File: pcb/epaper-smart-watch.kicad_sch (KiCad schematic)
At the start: 64 parts, among them J1 AXT624124, J3 Lithium Battery 3.7V, M1 Motor_DC, P1 USB_C_Plug_USB2.0, Q1 MMBT3904, Q3 Si1308EDL, SW1 BTN, SW2 BTN, SW3 BTN, SW4 BTN, U1 CH340E, U2 STM32WB1MMCH6TR, U3 LSM6DS3

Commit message: V2 soon...
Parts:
- removed C12: 4.7uF, Capacitor_SMD:C_0402_1005Metric, symbol Device:C_Small
- removed C13: 2.2uF, Capacitor_SMD:C_0402_1005Metric, symbol Device:C_Small
- removed C14: 1uF, Capacitor_SMD:C_0402_1005Metric, symbol Device:C_Small
- removed C15, C17, C9: 0.1uF, Capacitor_SMD:C_0402_1005Metric, symbol Device:C_Small
- removed C18: 10uF, Capacitor_SMD:C_0402_1005Metric, symbol Device:C_Small
- removed C19, C20, C21: 2.7pF, Capacitor_SMD:C_0402_1005Metric, symbol Device:C_Small
- removed D1, D3, D4: LESD5D5.0CT1G, SamacSys:LESD5D50CT1G, symbol SamacSys:LESD5D5.0CT1G
- removed D6: LED, LED_SMD:LED_0603_1608Metric, symbol Device:LED
- removed JP3: SolderJumper_3_Bridged12, Jumper:SolderJumper-3_P1.3mm_Bridged12_RoundedPad1.0x1.5mm_NumberLabels, symbol Jumper:SolderJumper_3_Bridged12
- removed PS1: STNS01PUR, SamacSys:SON45P300X300X80-13N-D, symbol SamacSys:STNS01PUR
- removed Q1: MMBT3904, Package_TO_SOT_SMD:SOT-23, symbol Transistor_BJT:MMBT3904
- removed R9: 2k, Resistor_SMD:R_0402_1005Metric, symbol Device:R_Small_US
- removed SWD1: JST-ZH6, Connector_JST:JST_ZE_SM06B-ZESS-TB_1x06-1MP_P1.50mm_Horizontal, symbol controller-eagle-import:JST-ZH6
- removed U1: CH340E, Package_SO:MSOP-10_3x3mm_P0.5mm, symbol Interface_USB:CH340E
- removed U2: STM32WB1MMCH6TR, EasyEda2Kicad:LGA-77_L10.0-W6.5-STM32WB1MMCH6TR, symbol Easy:STM32WB1MMCH6TR
- removed U3: LSM6DS3, Package_LGA:LGA-14_3x2.5mm_P0.5mm_LayoutBorder3x4y, symbol Sensor_Motion:LSM6DS3
- added AC1: BMA400, Package_LGA:LGA-12_2x2mm_P0.5mm, symbol SamasSys:BMA400
- added BZ1: Buzzer, Jumper:SolderJumper-2_P1.3mm_Open_Pad1.0x1.5mm, symbol Device:Buzzer
- added C10: 0.1uF, Capacitor_SMD:C_0402_1005Metric, symbol Device:C_Small
- added C11, C6: 100nF, Capacitor_SMD:C_0402_1005Metric, symbol Device:C_Small
- added C2, C3, C4: 10uF, Capacitor_SMD:C_0603_1608Metric, symbol Device:C_Small
- added C7: 2.2uF, Capacitor_SMD:C_0402_1005Metric, symbol Device:C_Small
- added C8: 1uF, Capacitor_SMD:C_0402_1005Metric, symbol Device:C_Small
- added D1, D3: LED, LED_SMD:LED_0603_1608Metric, symbol Device:LED
- added D6: MBR0530, Diode_SMD:D_SOD-123, symbol Device:D_Schottky
- added IC2: NPM1100-QDAA-R7, SamasSys:QFN50P400X400X90-25N-D, symbol SamasSys:NPM1100-QDAA-R7
- added IC3: MAX17048G+T10, SamasSys:SON50P200X200X80-9N-D, symbol SamasSys:MAX17048G+T10
- added IC4: AP3032, SamasSys:SOT95P280X145-6N, symbol SamasSys:AP3032
- added J10, J11, J12, J13, J14, J15, J4, J7, J8, J9: (no value), TestPoint:TestPoint_Pad_D1.0mm, symbol Connector:Conn_01x01_Pin
- added J16: Touch3, TestPoint:TestPoint_Pad_D1.0mm, symbol Connector:Conn_01x01_Pin
- added J17: Touch2, TestPoint:TestPoint_Pad_D1.0mm, symbol Connector:Conn_01x01_Pin
- added J18: Touch1, TestPoint:TestPoint_Pad_D1.0mm, symbol Connector:Conn_01x01_Pin
- added L1: 2.2uH, Inductor_SMD:L_0603_1608Metric, symbol Device:L
- added L3: 6.8uH, Inductor_SMD:L_0603_1608Metric, symbol Device:L
- added Q3: AO3400A, Package_TO_SOT_SMD:SOT-23, symbol Transistor_FET:AO3400A
- added R10: 750k, Resistor_SMD:R_0402_1005Metric, symbol Device:R_Small_US
- added R11, R12, R8: 100k, Resistor_SMD:R_0402_1005Metric, symbol Device:R_Small_US
- added R13, R6: 1k, Resistor_SMD:R_0402_1005Metric, symbol Device:R_Small_US
- added SW6: SW_Push, Button_Switch_SMD:SW_SPST_TS-1088-xR020, symbol Switch:SW_Push
- added SWD1: JST-ZH6, Connector_JST:JST_ZE_SM06B-ZESS-TB_1x06-1MP_P1.50mm_Horizontal, symbol Connector_Generic:Conn_01x06
- added U1: BME280, Package_LGA:Bosch_LGA-8_2.5x2.5mm_P0.65mm_ClockwisePinNumbering, symbol Sensor:BME280
- added U2: USBLC6-2SC6, Package_TO_SOT_SMD:SOT-23-6, symbol Power_Protection:USBLC6-2SC6
- added U3: STM32WB5MMG, RF_Module:ST-SiP-LGA-86-11x7.3mm, symbol RF_Module:STM32WB5MMG
- added U4: XT25F32FDTIGT, ProjectLibrary:DFN-8_L3.0-W2.0-P0.50-BL-EP_XT25XXX, symbol ProjectLibrary:XT25F32FDTIGT
- C13: renamed from C1; footprint Capacitor_SMD:C_0402_1005Metric -> Capacitor_SMD:C_0603_1608Metric
- C16: value 4.7uF -> 1uF; footprint Capacitor_SMD:C_0402_1005Metric -> Capacitor_SMD:C_0603_1608Metric; Distributor 1 490-10730-1-ND -> (none); Manufacturer Murata Electronics North America -> (none); Manufacturer Part GRM188R61C475KE11D -> (none)
- C21: renamed from C4; footprint Capacitor_SMD:C_0402_1005Metric -> Capacitor_SMD:C_0603_1608Metric
- C22: value 2.2uF -> 10uF; footprint Capacitor_SMD:C_0402_1005Metric -> Capacitor_SMD:C_0603_1608Metric
- C24, C25: value 0.1uF -> 100nF
- J6: renamed from J1; footprint FPC:AXT624124 -> ProjectLibrary:AXT624124
- P1: footprint USBC:USB-C-SMD_KH-TYPE-C-16P -> ProjectLibrary:USB-C-SMD_TYPE-C-16P-CB0.8-073; symbol Connector:USB_C_Receptacle_USB2.0 -> Connector:USB_C_Receptacle_USB2.0_14P
- Q2: renamed from Q3; footprint Package_TO_SOT_SMD:SOT-323_SC-70 -> Package_TO_SOT_SMD:SOT-23
- R1: value 2k -> 10k
- R14: value 1k -> 100k
- R15: value 1k -> 10
- R16: value 1k -> 10k
- R2: value 10K -> 10k
- R5: value 600 -> 8.2k
- R7: value 10K -> 100
- renumbered C2 to C12, C8 to C14, C3 to C15, C11 to C17, C7 to C18, C6 to C19, C5 to C20, C10 to C23, C23 to C9, D9 to D4, D7 to D5, D5 to D7, J3 to J5, L1 to L2, R6 to R9, SW1 to SW2, SW2 to SW3, SW3 to SW4, SW4 to SW5
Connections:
- net Accel_SDA is gone; now on net VIB: R7.2
- net TXD is gone; now on net GND: JP1.2 (C)
- net BTN_1: now also U3.22 (PC10)
- net BTN_2: now also U3.23 (PC11)
- net BTN_3: now also U3.24 (PC12)
- net BTN_4: now also U3.20 (PB4)
- net D+: now also IC2.20 (D+), U2.4 (I/O2), U3.29 (PA12); no longer P1.A6 (D+), P1.B6 (D+)
- net D-: now also IC2.19 (D-), U2.6 (I/O1), U3.30 (PA11); no longer P1.A7 (D-), P1.B7 (D-)
- net EPD_MOSI: now also J10.1 (Pin_1), U3.52 (PA7)
- net EPD_SPICL: now also J11.1 (Pin_1), U3.54 (PA5)
- net GND: now also C24.1, C25.1, J5.3 (Pin_3), P1.SH (SHIELD), R15.1, R16.2, R5.1, AC1.1 (SDO), AC1.8 (GNDIO), AC1.9 (GND), BZ1.2 (-), C10.2, C11.2, C2.2, C3.2, C4.2, C6.1, C7.2, C8.2, D3.1 (K), IC2.23 (PVSS), IC2.25 (GND), IC3.1 (CTG), IC3.4 (GND), IC3.6 (QSTRT), IC3.9 (EP), IC4.2 (GND), Q3.2 (S), R12.1, R13.1, R8.2, SWD1.4 (Pin_4), U1.1 (GND), U1.5 (SDO), U1.7 (GND), U2.2 (GND), U3.16 (VSSSMPS), U3.31 (VSS), U3.5 (VSS), U3.57 (VSS), U3.58 (ANT_IN), U3.59 (RF_OUT), U3.60 (VSS), U3.84 (VSS), U3.86 (VSS), U4.4 (VSS), U4.9 (EP); no longer C16.2, C24.2, C25.2, C9.2, D4.2 (A), J5.2 (Pin_2), M1.2 (-), P1.S1 (SHIELD)
- net NRST: now also C24.2, SWD1.2 (Pin_2), U3.10 (NRST)
- net SWDCLK: now also SWD1.5 (Pin_5), U3.26 (PA14)
- net SWDIO: now also SWD1.3 (Pin_3), U3.25 (PA13)
- net VIB: now also U3.27 (PA15)
- net +3V0: now reaches R14.1
- net +3V0: now also C12.1, C13.1, C22.1, J6.9 (Pin_9), JP1.3 (B), L2.1, R1.1, R2.1, AC1.10 (CSB), AC1.3 (VDDIO), AC1.7 (VDD), C11.1, C2.1, C6.2, IC2.1 (VOUTB), IC4.6 (VIN), L1.2, L3.2, SW6.1, SWD1.6 (Pin_6), U1.2 (CSB), U1.6 (VDDIO), U1.8 (VDD), U3.15 (VBAT), U3.17 (VDDSMPS), U3.32 (VDDUSB), U3.4 (VREF), U3.6 (VDDA), U4.8 (VCC)
- net FLASH_CS: now reaches R14.2
- net FLASH_CS: now also U3.70 (PD3), U4.1 (~{CS})
- net at R16.1: now also JP2.1 (A)
- net ACCL_SDA: now reaches R1.2
- net ACCL_SDA: now also AC1.2 (SDX), IC3.8 (SDA), U1.3 (SDI), U3.11 (PB9)
- net at J5.1 (Pin_1): now also C10.1, C8.1, IC2.15 (VBAT), IC3.2 (CELL), IC3.3 (VDD)
- net VSYS: now reaches C9.1, D4.1 (K), M1.1 (+)
- net VSYS: now also D2.2 (A), C4.1, D1.2 (A), IC2.16 (VSYS), IC2.2 (VOUTBSET1), IC2.3 (VOUTBSET2), IC2.9 (VTERMSET)
- net at J6.16 (Pin_16): now also JP1.1 (A)
- net at R5.2: now also IC2.12 (ICHG); no longer D2.2 (A)
- net Accel_SCL renamed ACCL_SCL
- net ACCL_SCL: now also AC1.12 (SCX), IC3.7 (SCL), U1.4 (SCK), U3.14 (PB8)
- net BUSY renamed EPD_BUSY
- net EPD_BUSY: now also J15.1 (Pin_1), U3.1 (PA2)
- net CHG: no longer names the net of D2.1 (K)
- net CHG: now also IC2.8 (CHG)
- net CSB renamed EPD_CSB
- net EPD_CSB: now also J12.1 (Pin_1), U3.55 (PA4)
- net DC renamed EPD_DC
- net EPD_DC: now also J13.1 (Pin_1), U3.50 (PA8)
- removed net EPD_VDD: C12.1, C13.1, C16.1, C24.1, C25.1, J6.9 (Pin_9), L2.1, R2.1, R5.1, R7.1
- net FL+ renamed EPD_LIGHT_PWR_POS
- net EPD_LIGHT_PWR_POS: now also C16.1, D6.1 (K), R10.1
- net FL- renamed EPD_LIGHT_PWR_NEG
- net EPD_LIGHT_PWR_NEG: now also C16.2, R15.2, IC4.3 (FB), R11.2
- net GDR renamed EPD_GDR
- net EPD_GDR: now also R12.2
- net RESR renamed EPD_RESR
- net RST_N renamed EPD_RST_N
- net EPD_RST_N: now also J14.1 (Pin_1), U3.53 (PA6)
- net RXD: no longer names the net of JP2.2 (C)
- net RXD: now also IC2.14 (NTC)
- net VBUS renamed +5V
- net +5V: now also C7.1, IC2.17 (VBUS), R6.1, U2.5 (VBUS)
- net VCOM renamed EPD_VCOM
- net EPD_VCOM: now also J7.1 (Pin_1)
- net VGH renamed EPD_VGH
- net EPD_VGH: now also J9.1 (Pin_1)
- net VGL renamed EPD_VGL
- net EPD_VGL: now also J8.1 (Pin_1)
- new net: Q3.1 (G), R7.1, R8.1
- new net: C25.2, U3.40 (PC13)
- new net: IC2.6 (SHPACT), J4.1 (Pin_1)
- new net: SW6.2, U3.13 (PH3-BOOT0)
- new net: IC4.5 (OV), R10.2, R11.1
- new net: C3.1, IC2.21 (DEC)
- new net: D3.2 (A), R6.2
- new net: J18.1 (Pin_1), U3.41 (PB12)
- new net: J17.1 (Pin_1), U3.35 (PB13)
- new net: D1.1 (K), IC2.10 (ERR)
- new net: J5.2 (Pin_2), JP2.3 (B)
- new net: J16.1 (Pin_1), U3.37 (PB14)
- new net: IC2.22 (SW), L1.1
- new net: P1.A6 (D+), P1.B6 (D+), U2.3 (I/O2)
- new net: P1.A7 (D-), P1.B7 (D-), U2.1 (I/O1)
- new net: C9.2, D4.2 (A), M1.2 (-), Q3.3 (D)
- new net: D6.2 (A), IC4.1 (SW), L3.1
- new net ACCL_INT1: AC1.5 (INT1), U3.12 (PC0)
- new net ACCL_INT2: AC1.6 (INT2), U3.9 (PC1)
- new net BATC_ALRT: IC3.5 (~{ALRT}), U3.21 (PB3)
- new net CHGR_ISET: IC2.5 (ISET), U3.33 (PD0)
- new net CHGR_MODE: IC2.7 (MODE), R13.2, U3.51 (PA9)
- new net CHGR_SHPHLD: IC2.11 (SHPHLD), U3.36 (PC6)
- new net EPD_LIGHT: IC4.4 (CTRL), U3.64 (PE1)
- new net FLASH_CLK: U3.56 (PA3), U4.6 (SCLK)
- new net FLASH_IO0: U3.73 (PD4), U4.5 (SI(IO0))
- new net FLASH_IO1: U3.80 (PD5), U4.2 (SO(IO1))
- new net FLASH_IO2: U3.81 (PD6), U4.3 (WP#(IO2))
- new net FLASH_IO3: U3.67 (PD7), U4.7 (HOLD#(IO3))
- new net SND: BZ1.1 (+), U3.79 (PE0)
- no-connect marks 13 -> 44
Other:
- note removed: "4k for 100mAh"
- moved on the sheet: C12, C13, C14, C15, C17, C18, C19, C20, C21, C23, C9, D4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

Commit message: Routed the board, will do verification check soon
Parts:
- P1: footprint ProjectLibrary:USB-C-SMD_TYPE-C-16P-CB0.8-073 -> ProjectLibrary:USB-C-SMD_SHOU_TYPE-C-16P-CB1.6
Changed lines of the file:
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@@
 			)
 		)
-		(property "Footprint" "ProjectLibrary:USB-C-SMD_TYPE-C-16P-CB0.8-073"
+		(property "Footprint" "ProjectLibrary:USB-C-SMD_SHOU_TYPE-C-16P-CB1.6"
 			(at 48.26 63.5 0)
 			(hide yes)

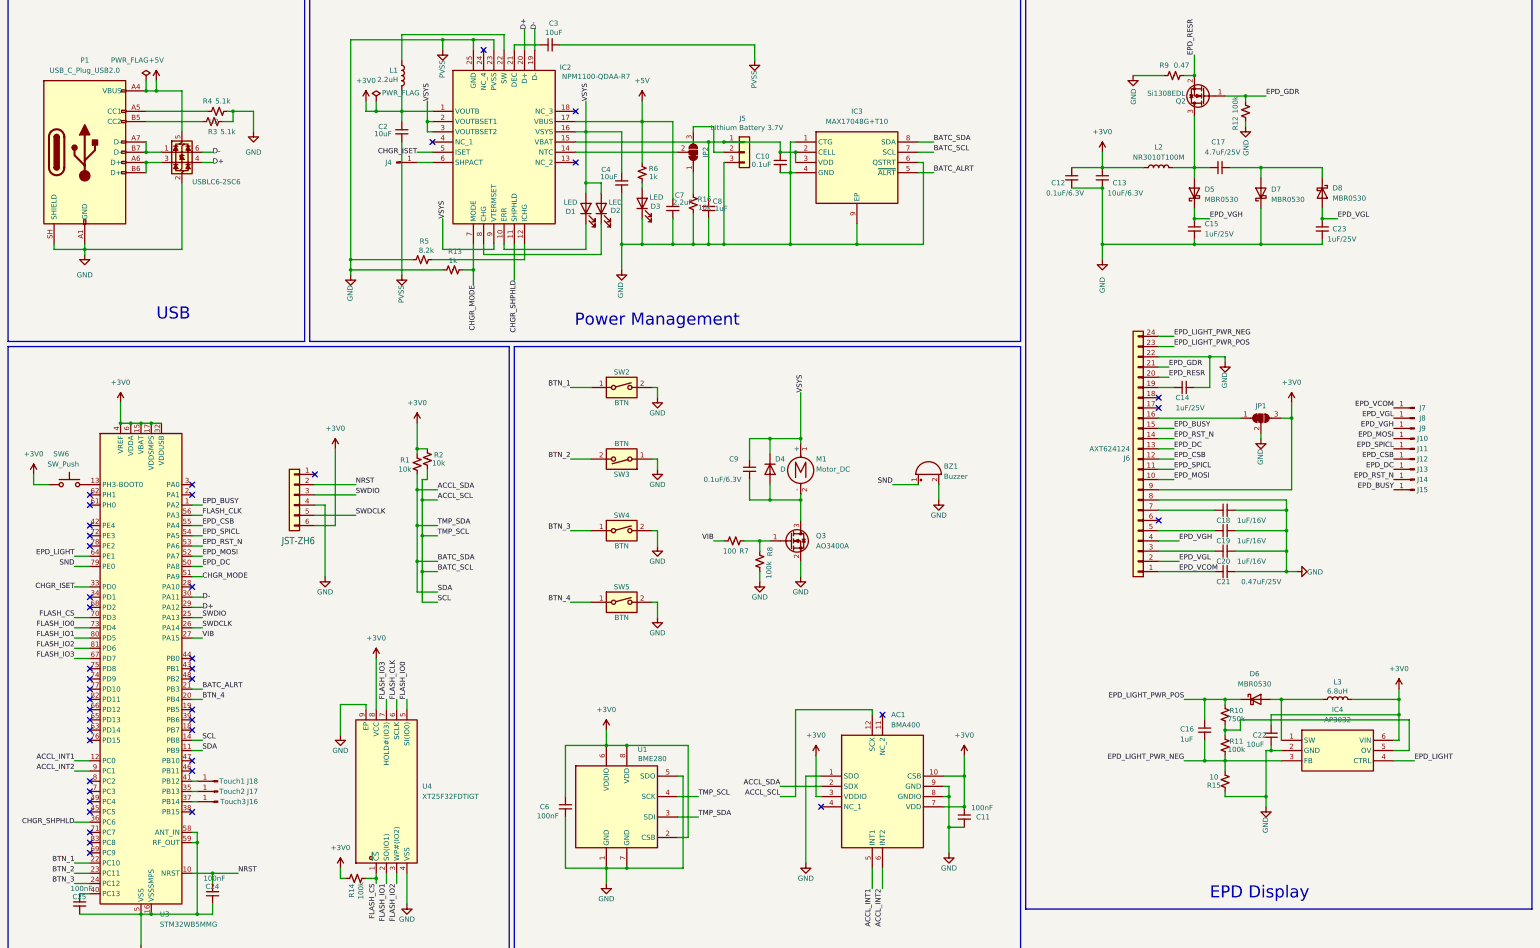
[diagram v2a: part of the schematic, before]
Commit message: Routed board
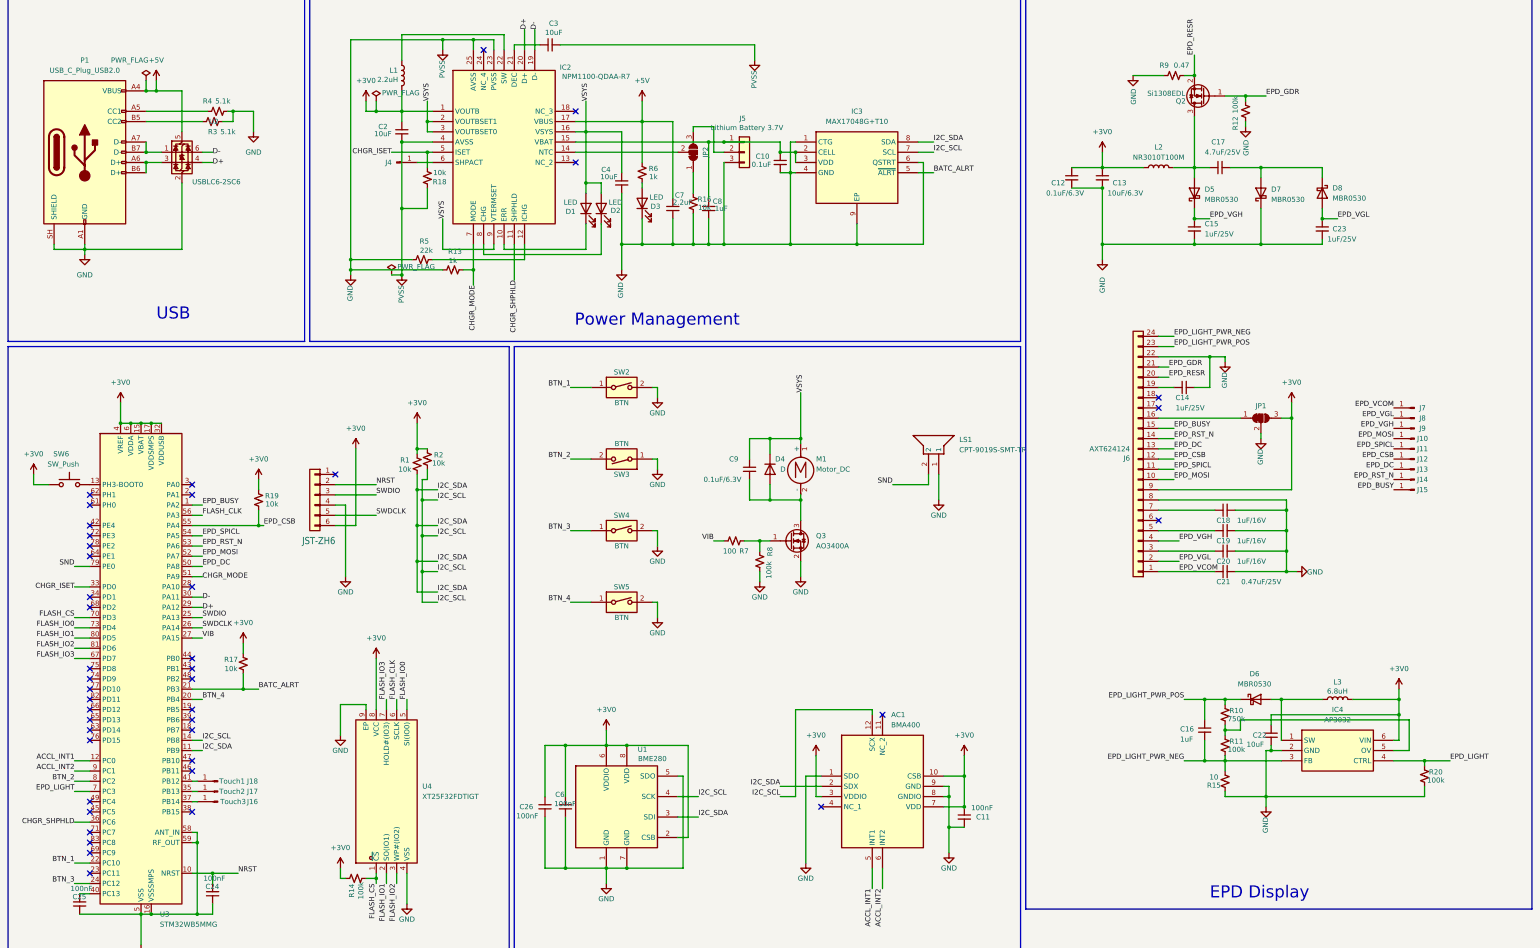
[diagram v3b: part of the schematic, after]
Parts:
- removed BZ1: Buzzer, Jumper:SolderJumper-2_P1.3mm_Open_Pad1.0x1.5mm, symbol Device:Buzzer
- added C26: 100nF, Capacitor_SMD:C_0402_1005Metric, symbol Device:C_Small
- added LS1: CPT-9019S-SMT-TR, CPT9019SSMTTR, symbol SamasSys:CPT-9019S-SMT-TR
- added R17, R18, R19: 10k, Resistor_SMD:R_0402_1005Metric, symbol Device:R_Small_US
- added R20: 100k, Resistor_SMD:R_0402_1005Metric, symbol Device:R_Small_US
- IC2: footprint SamasSys:QFN50P400X400X90-25N-D -> QFN50P400X400X90-25N-D
- L2: footprint Inductor_SMD:L_Taiyo-Yuden_NR-40xx -> Inductor_SMD:L_Taiyo-Yuden_NR-30xx
- Q2: footprint Package_TO_SOT_SMD:SOT-23 -> Package_TO_SOT_SMD:SOT-323_SC-70
- R5: value 8.2k -> 22k
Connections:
- net +3V0: now also C26.2, R17.1, R19.1
- net BATC_ALRT: now also R17.2
- net BTN_2: now also U3.8 (PC2); no longer U3.23 (PC11)
- net CHGR_ISET: now also R18.2
- net EPD_CSB: now also R19.2
- net EPD_LIGHT: now also U3.7 (PC3), R20.1; no longer U3.64 (PE1)
- net GND: now also IC2.4 (AVSS), C26.1, LS1.1, R18.1, R20.2
- net SND: now also LS1.2
- net ACCL_SCL renamed I2C_SCL
- net ACCL_SDA renamed I2C_SDA
- no-connect marks 44 -> 43

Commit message: Final production V2 ready
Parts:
- removed D4: D, Diode_SMD:D_SOD-323, symbol Device:D
- added C27, C5: 1uF/16V, Capacitor_SMD:C_0402_1005Metric, symbol Device:C_Small
- added D9: MBR0530, Diode_SMD:D_SOD-123, symbol Device:D_Schottky
- added Q4: AO3400A, Package_TO_SOT_SMD:SOT-23, symbol Transistor_FET:AO3400A
- added R21, R24: 1k, Resistor_SMD:R_0402_1005Metric, symbol Device:R_Small_US
- added R22: 100, Resistor_SMD:R_0402_1005Metric, symbol Device:R_Small_US
- added R23: 100k, Resistor_SMD:R_0402_1005Metric, symbol Device:R_Small_US
- added U5: XC6206P332MR, Package_TO_SOT_SMD:SOT-23-3, symbol Regulator_Linear:XC6206PxxxMR
- C14: footprint Capacitor_SMD:C_0402_1005Metric -> Capacitor_SMD:C_0603_1608Metric
- C16: value 1uF -> 1uF/16V
- C19, C20: value 1uF/16V -> 1uF/25V; footprint Capacitor_SMD:C_0402_1005Metric -> Capacitor_SMD:C_0603_1608Metric
- C7: value 2.2uF -> 2.2uF/25V; footprint Capacitor_SMD:C_0402_1005Metric -> Capacitor_SMD:C_0805_2012Metric
- C9: value 0.1uF/6.3V -> 0.1uF/16V
- IC2: footprint QFN50P400X400X90-25N-D -> SamasSys:QFN50P400X400X90-25N-D
- LS1: footprint CPT9019SSMTTR -> SamasSys:CPT9019SSMTTR
- R15: value 10 -> 100
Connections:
- net +3V0: now also R21.1; no longer C22.1, IC4.6 (VIN), L3.2, SW6.1, U3.32 (VDDUSB)
- net +5V: now also C5.1, U5.3 (VI)
- net GND: now also C25.2, JP1.1 (A), C27.1, C5.2, Q4.2 (S), R23.2, U5.1 (GND); no longer C25.1, JP1.2 (C), LS1.1
- net SND: now also R22.2; no longer LS1.2
- net VSYS: now also C22.1, IC4.6 (VIN), L3.2, LS1.2, D9.1 (K), R24.1
- net at U3.40 (PC13): no longer C25.2
- net at J18.1 (Pin_1): now also U3.35 (PB13); no longer U3.41 (PB12)
- net at J17.1 (Pin_1): now also U3.37 (PB14); no longer U3.35 (PB13)
- net at J16.1 (Pin_1): now also U3.38 (PB15); no longer U3.37 (PB14)
- net at C9.2, M1.2 (-), Q3.3 (D): now also D9.2 (A)
- net at J6.16 (Pin_16): now also JP1.2 (C); no longer JP1.1 (A)
- new net: R21.2, SW6.1
- new net: LS1.1, Q4.3 (D), R24.2
- new net: C25.1, U3.41 (PB12)
- new net: Q4.1 (G), R22.1, R23.1
- new net VUSB: C27.2, U3.32 (VDDUSB), U5.2 (VO)
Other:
- moved on the sheet: C24, C9, M1, P1, Q3, R3, R4, R7, R8, U2
